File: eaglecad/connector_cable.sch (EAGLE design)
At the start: 2 parts

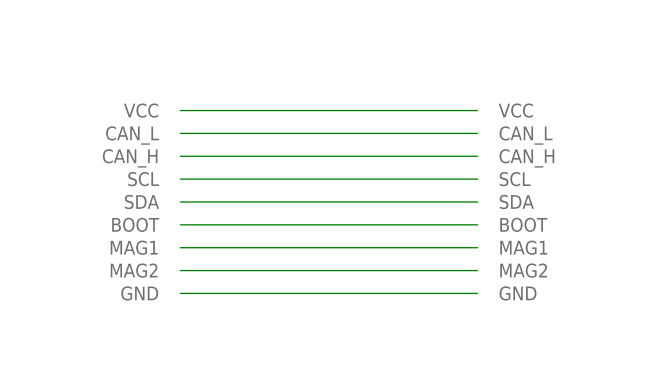
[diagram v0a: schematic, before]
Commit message: Flex cable prototype
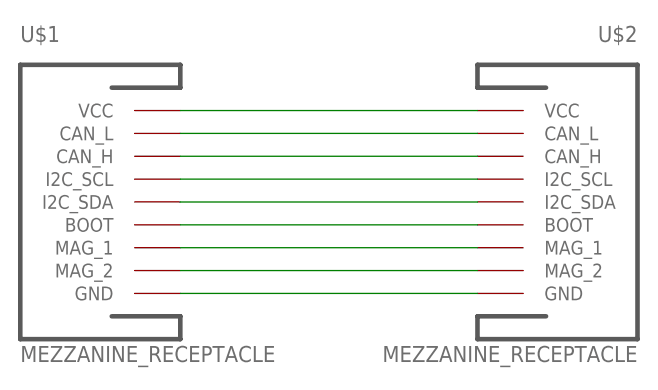
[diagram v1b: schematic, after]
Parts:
- removed U$3: FLEX-DRIVER_CONN, oresat-ACS_driver_board:FLEX-DRIVER_CONN
- added U$1: MEZZANINE_RECEPTACLE, oresat-ACS_driver_board:MEZZANINE_RECEPTACLE
- U$2: value FLEX-CARD_CONN -> MEZZANINE_RECEPTACLE; device oresat-ACS_driver_board:FLEX-CARD_CONN -> oresat-ACS_driver_board:MEZZANINE_RECEPTACLE
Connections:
- net BOOT: now also U$1.BOOT; no longer U$3.BOOT
- net CAN_H: now also U$1.CAN_H; no longer U$3.CAN_H
- net CAN_L: now also U$1.CAN_L; no longer U$3.CAN_L
- net GND: now also U$1.GND; no longer U$3.GND
- net MAG1: now also U$1.MAG_1, U$2.MAG_1; no longer U$2.MAG1, U$3.MAG1
- net MAG2: now also U$1.MAG_2, U$2.MAG_2; no longer U$2.MAG2, U$3.MAG2
- net SCL: now also U$1.I2C_SCL, U$2.I2C_SCL; no longer U$2.SCL, U$3.SCL
- net SDA: now also U$1.I2C_SDA, U$2.I2C_SDA; no longer U$2.SDA, U$3.SDA
- net VCC: now also U$1.VCC; no longer U$3.VCC
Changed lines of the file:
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@@
 </classes>
 <parts>
-<part name="U$2" library="oresat-ACS_driver_board" deviceset="FLEX-CARD_CONN" device=""/>
-<part name="U$3" library="oresat-ACS_driver_board" deviceset="FLEX-DRIVER_CONN" device=""/>
 <part name="FRAME1" library="frames" library_urn="urn:adsk.eagle:library:229" deviceset="DINA5_L" device=""/>
+<part name="U$1" library="oresat-ACS_driver_board" deviceset="MEZZANINE_RECEPTACLE" device=""/>
+<part name="U$2" library="oresat-ACS_driver_board" deviceset="MEZZANINE_RECEPTACLE" device=""/>
 </parts>
 <sheets>
@@
 </plain>
 <instances>
-<instance part="U$2" gate="G$1" x="101.6" y="68.58" smashed="yes"/>
-<instance part="U$3" gate="G$1" x="68.58" y="68.58" smashed="yes" rot="MR0"/>
 <instance part="FRAME1" gate="G$1" x="0" y="0" smashed="yes">
 <attribute name="DRAWING_NAME" x="140.97" y="15.24" size="2.54" layer="94"/>
 <attribute name="LAST_DATE_TIME" x="140.97" y="10.16" size="2.286" layer="94"/>
 <attribute name="SHEET" x="154.305" y="5.08" size="2.54" layer="94"/>
+</instance>
+<instance part="U$1" gate="G$1" x="63.5" y="68.58" smashed="yes">
+<attribute name="NAME" x="50.8" y="86.36" size="1.778" layer="95"/>
+<attribute name="VALUE" x="50.8" y="50.8" size="1.778" layer="96"/>
+</instance>
+<instance part="U$2" gate="G$1" x="106.68" y="68.58" smashed="yes" rot="MR0">
+<attribute name="NAME" x="119.38" y="86.36" size="1.778" layer="95" rot="MR0"/>
+<attribute name="VALUE" x="119.38" y="50.8" size="1.778" layer="96" rot="MR0"/>
 </instance>
 </instances>
@@
 <net name="VCC" class="0">
 <segment>
-<pinref part="U$3" gate="G$1" pin="VCC"/>
+<wire x1="68.58" y1="78.74" x2="101.6" y2="78.74" width="0.1524" layer="91"/>
+<pinref part="U$1" gate="G$1" pin="VCC"/>
 <pinref part="U$2" gate="G$1" pin="VCC"/>
-<wire x1="68.58" y1="78.74" x2="101.6" y2="78.74" width="0.1524" layer="91"/>
 </segment>
 </net>
 <net name="CAN_L" class="0">
 <segment>
+<wire x1="101.6" y1="76.2" x2="68.58" y2="76.2" width="0.1524" layer="91"/>
+<pinref part="U$1" gate="G$1" pin="CAN_L"/>
 <pinref part="U$2" gate="G$1" pin="CAN_L"/>
-<pinref part="U$3" gate="G$1" pin="CAN_L"/>
-<wire x1="101.6" y1="76.2" x2="68.58" y2="76.2" width="0.1524" layer="91"/>
 </segment>
 </net>
 <net name="CAN_H" class="0">
 <segment>
-<pinref part="U$3" gate="G$1" pin="CAN_H"/>
+<wire x1="68.58" y1="73.66" x2="101.6" y2="73.66" width="0.1524" layer="91"/>
+<pinref part="U$1" gate="G$1" pin="CAN_H"/>
 <pinref part="U$2" gate="G$1" pin="CAN_H"/>
-<wire x1="68.58" y1="73.66" x2="101.6" y2="73.66" width="0.1524" layer="91"/>
 </segment>
 </net>
 <net name="SCL" class="0">
 <segment>
-<pinref part="U$2" gate="G$1" pin="SCL"/>
-<pinref part="U$3" gate="G$1" pin="SCL"/>
 <wire x1="101.6" y1="71.12" x2="68.58" y2="71.12" width="0.1524" layer="91"/>
+<pinref part="U$1" gate="G$1" pin="I2C_SCL"/>
+<pinref part="U$2" gate="G$1" pin="I2C_SCL"/>
 </segment>
 </net>
 <net name="SDA" class="0">
 <segment>
-<pinref part="U$3" gate="G$1" pin="SDA"/>
-<pinref part="U$2" gate="G$1" pin="SDA"/>
 <wire x1="68.58" y1="68.58" x2="101.6" y2="68.58" width="0.1524" layer="91"/>
+<pinref part="U$1" gate="G$1" pin="I2C_SDA"/>
+<pinref part="U$2" gate="G$1" pin="I2C_SDA"/>
 </segment>
 </net>
 <net name="BOOT" class="0">
 <segment>
+<wire x1="101.6" y1="66.04" x2="68.58" y2="66.04" width="0.1524" layer="91"/>
+<pinref part="U$1" gate="G$1" pin="BOOT"/>
 <pinref part="U$2" gate="G$1" pin="BOOT"/>
-<pinref part="U$3" gate="G$1" pin="BOOT"/>
-<wire x1="101.6" y1="66.04" x2="68.58" y2="66.04" width="0.1524" layer="91"/>
 </segment>
 </net>
 <net name="MAG1" class="0">
 <segment>
-<pinref part="U$3" gate="G$1" pin="MAG1"/>
-<pinref part="U$2" gate="G$1" pin="MAG1"/>
 <wire x1="68.58" y1="63.5" x2="101.6" y2="63.5" width="0.1524" layer="91"/>
+<pinref part="U$1" gate="G$1" pin="MAG_1"/>
+<pinref part="U$2" gate="G$1" pin="MAG_1"/>
 </segment>
 </net>
 <net name="MAG2" class="0">
 <segment>
-<pinref part="U$2" gate="G$1" pin="MAG2"/>
-<pinref part="U$3" gate="G$1" pin="MAG2"/>
 <wire x1="101.6" y1="60.96" x2="68.58" y2="60.96" width="0.1524" layer="91"/>
+<pinref part="U$1" gate="G$1" pin="MAG_2"/>
+<pinref part="U$2" gate="G$1" pin="MAG_2"/>
 </segment>
 </net>
 <net name="GND" class="0">
 <segment>
-<pinref part="U$3" gate="G$1" pin="GND"/>
+<wire x1="68.58" y1="58.42" x2="101.6" y2="58.42" width="0.1524" layer="91"/>
+<pinref part="U$1" gate="G$1" pin="GND"/>
 <pinref part="U$2" gate="G$1" pin="GND"/>
-<wire x1="68.58" y1="58.42" x2="101.6" y2="58.42" width="0.1524" layer="91"/>
 </segment>
 </net>
